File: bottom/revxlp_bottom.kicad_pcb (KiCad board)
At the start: 2 copper layers, 238.7 x 92.9 mm, 9 parts

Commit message: Initial 3dp case work.
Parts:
- moved H3 18.3 mm to (64.5, 99.7)
- moved H5 18.3 mm to (181.2, 125.8)
- moved H6 18.3 mm to (224.8, 99.7)
- moved H1 18.3 mm to (72.1, 66.2)
- moved H2 18.3 mm to (217.2, 66.2)
- moved rev41lp_edgecutPCB 18.3 mm to (144.6, 62.0)
- moved G*** 18.3 mm to (152.3, 67.1)
- moved H4 18.3 mm to (107.6, 126.2)
- moved H7 18.3 mm to (144.6, 78.1)
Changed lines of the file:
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@@
     )
     (pad_to_mask_clearance 0)
-    (aux_axis_origin 142.816164 156.58206)
     (grid_origin 110.242222 -34.443781)
     (pcbplotparams
-      (layerselection 0x00010fc_ffffffff)
+      (layerselection 0x0001000_7ffffffe)
       (disableapertmacros false)
       (usegerberextensions true)
@@
       (hpglpenspeed 20)
       (hpglpendiameter 15.000000)
-      (dxfpolygonmode true)
-      (dxfimperialunits true)
+      (dxfpolygonmode false)
+      (dxfimperialunits false)
       (dxfusepcbnewfont true)
       (psnegative false)
@@
       (sketchpadsonfab false)
       (subtractmaskfromsilk true)
-      (outputformat 1)
+      (outputformat 3)
       (mirror false)
       (drillshape 0)
       (scaleselection 1)
-      (outputdirectory "./")
+      (outputdirectory "./dxf")
     )
   )
@@
   (net 2 "+5V")
   (footprint "revxlp:rev41lp_edgecutBottomPlate" (layer "F.Cu")
-    (at 144.871005 43.697242)
+    (at 144.639118 61.979835)
     (attr through_hole)
     (fp_text reference "rev41lp_edgecutPCB" (at 0 0.5) (layer "F.SilkS") hide
@@
     (fp_arc (start -109.584369 0.795048) (mid -109.232514 0.237391) (end -108.61 0.019999) (layer "Edge.Cuts") (width 0.2))
     (fp_arc (start -55.237421 0.019999) (mid -52.973357 0.148562) (end -50.7384 0.532597) (layer "Edge.Cuts") (width 0.2))
-    (fp_arc (start 19.732403 86.445868) (mid 17.497445 86.829902) (end 15.233381 86.958468) (layer "Edge.Cuts") (width 0.2))
+    (fp_arc (start 19.732403 86.445868) (mid 17.497446 86.829906) (end 15.233381 86.958468) (layer "Edge.Cuts") (width 0.2))
     (fp_arc (start -100.034262 53.761991) (mid -102.298326 53.633428) (end -104.533283 53.249393) (layer "Edge.Cuts") (width 0.2))
     (fp_arc (start -17.78846 86.958467) (mid -20.052524 86.829904) (end -22.287481 86.445868) (layer "Edge.Cuts") (width 0.2))
@@
     (fp_arc (start 55.327513 75.76074) (mid 55.034606 76.467826) (end 54.327513 76.76074) (layer "Edge.Cuts") (width 0.2))
     (fp_arc (start -86.118211 53.76199) (mid -83.854147 53.890553) (end -81.619191 54.27459) (layer "Edge.Cuts") (width 0.2))
-    (fp_arc (start 48.183323 0.532598) (mid 50.418279 0.148565) (end 52.682343 0.02) (layer "Edge.Cuts") (width 0.2))
+    (fp_arc (start 48.183323 0.532598) (mid 50.418279 0.14856) (end 52.682343 0.02) (layer "Edge.Cuts") (width 0.2))
     (fp_arc (start 118.045976 48.513551) (mid 117.919653 49.268421) (end 117.296557 49.712872) (layer "Edge.Cuts") (width 0.2))
-    (fp_arc (start 101.978204 53.249393) (mid 99.743247 53.633427) (end 97.479183 53.761992) (layer "Edge.Cuts") (width 0.2))
+    (fp_arc (start 101.978204 53.249393) (mid 99.743248 53.633439) (end 97.479183 53.761992) (layer "Edge.Cuts") (width 0.2))
     (fp_arc (start 106.05492 0.019999) (mid 106.677424 0.237398) (end 107.029291 0.795047) (layer "Edge.Cuts") (width 0.2))
     (fp_arc (start 55.327512 60.550052) (mid 55.544915 59.927541) (end 56.102561 59.575682) (layer "Edge.Cuts") (width 0.2))
     (fp_arc (start -40.031514 82.349335) (mid -40.51367 82.082072) (end -40.780933 81.599916) (layer "Edge.Cuts") (width 0.2))
     (fp_arc (start -1.387482 -5.210371) (mid -0.943031 -5.833468) (end -0.188161 -5.959791) (layer "Edge.Cuts") (width 0.2))
-    (fp_arc (start 38.502691 2.749566) (mid 38.066137 2.799018) (end 37.628944 2.755581) (layer "Edge.Cuts") (width 0.2))
+    (fp_arc (start 38.502691 2.749566) (mid 38.066137 2.799039) (end 37.628944 2.755581) (layer "Edge.Cuts") (width 0.2))
     (fp_arc (start -4.911415 10.073644) (mid -5.353397 10.705476) (end -6.113507 10.835067) (layer "Edge.Cuts") (width 0.2))
-    (fp_arc (start 39.164133 77.535789) (mid 39.515979 76.978113) (end 40.138502 76.76074) (layer "Edge.Cuts") (width 0.2))
+    (fp_arc (start 39.164133 77.535789) (mid 39.516018 76.978179) (end 40.138502 76.76074) (layer "Edge.Cuts") (width 0.2))
     (fp_arc (start -42.693581 76.760738) (mid -42.071066 76.97813) (end -41.71921 77.535788) (layer "Edge.Cuts") (width 0.2))
   )
   (footprint "MountingHole:MountingHole_3.2mm_M3" (layer "B.Cu")
-    (at 225.018875 81.383061 180)
+    (at 224.786988 99.665654 180)
     (descr "Mounting Hole 3.2mm, no annular, M3")
     (tags "mounting hole 3.2mm no annular m3")
@@
   )
   (footprint "MountingHole:MountingHole_3.2mm_M3" (layer "B.Cu")
-    (at 144.87101 59.788938 180)
+    (at 144.639123 78.071531 180)
     (descr "Mounting Hole 3.2mm, no annular, M3")
     (tags "mounting hole 3.2mm no annular m3")
@@
   )
   (footprint "MountingHole:MountingHole_3.2mm_M3" (layer "B.Cu")
-    (at 107.842305 107.868103 180)
+    (at 107.610418 126.150696 180)
     (descr "Mounting Hole 3.2mm, no annular, M3")
     (tags "mounting hole 3.2mm no annular m3")
@@
   )
   (footprint "MountingHole:MountingHole_3.2mm_M3" (layer "B.Cu")
-    (at 181.392308 107.468103 180)
+    (at 181.160421 125.750696 180)
     (descr "Mounting Hole 3.2mm, no annular, M3")
     (tags "mounting hole 3.2mm no annular m3")
@@
   )
   (footprint "MountingHole:MountingHole_3.2mm_M3" (layer "B.Cu")
-    (at 217.400305 47.893104 180)
+    (at 217.168418 66.175697 180)
     (descr "Mounting Hole 3.2mm, no annular, M3")
     (tags "mounting hole 3.2mm no annular m3")
@@
   )
   (footprint "revxlp:Z_Towel_Logo" (layer "B.Cu")
-    (at 152.579849 48.779431 -103)
+    (at 152.347962 67.062024 -103)
     (attr through_hole)
     (fp_text reference "G***" (at 0 0 77) (layer "B.SilkS") hide
@@
   )
   (footprint "MountingHole:MountingHole_3.2mm_M3" (layer "B.Cu")
-    (at 64.722623 81.383061 180)
+    (at 64.490736 99.665654 180)
     (descr "Mounting Hole 3.2mm, no annular, M3")
     (tags "mounting hole 3.2mm no annular m3")
@@
   )
   (footprint "MountingHole:MountingHole_3.2mm_M3" (layer "B.Cu")
-    (at 72.342303 47.893105 180)
+    (at 72.110416 66.175698 180)
     (descr "Mounting Hole 3.2mm, no annular, M3")
     (tags "mounting hole 3.2mm no annular m3")
@@
     (polygon
       (pts
-        (xy 255.21352 28.48898)
-        (xy 272.713517 29.488977)
-        (xy 274.213519 136.988983)
-        (xy 144.213519 141.238978)
-        (xy 12.213516 109.238982)
-        (xy 32.463518 25.738984)
+        (xy 254.981633 46.771573)
+        (xy 272.48163 47.77157)
+        (xy 273.981632 155.271576)
+        (xy 143.981632 159.521571)
+        (xy 11.981629 127.521575)
+        (xy 32.231631 44.021577)
       )
     )
@@
     (polygon
       (pts
-        (xy 254.120178 27.221259)
-        (xy 276.370171 136.471261)
-        (xy 11.120169 131.471257)
-        (xy 36.62018 23.721262)
+        (xy 253.888291 45.503852)
+        (xy 276.138284 154.753854)
+        (xy 10.888282 149.75385)
+        (xy 36.388293 42.003855)
       )
     )

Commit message: Fixes for bottom plate and 3dp case to actually match PCB, add bottom edge fillet/chamfer.
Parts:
- moved G*** 6.53 mm to (146.0, 65.5)
- moved H1 1.30 mm to (73.4, 66.2)
- moved H3 1.30 mm to (65.8, 99.7)
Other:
- board size 238.7 x 92.9 mm -> 238.7 x 94.8 mm

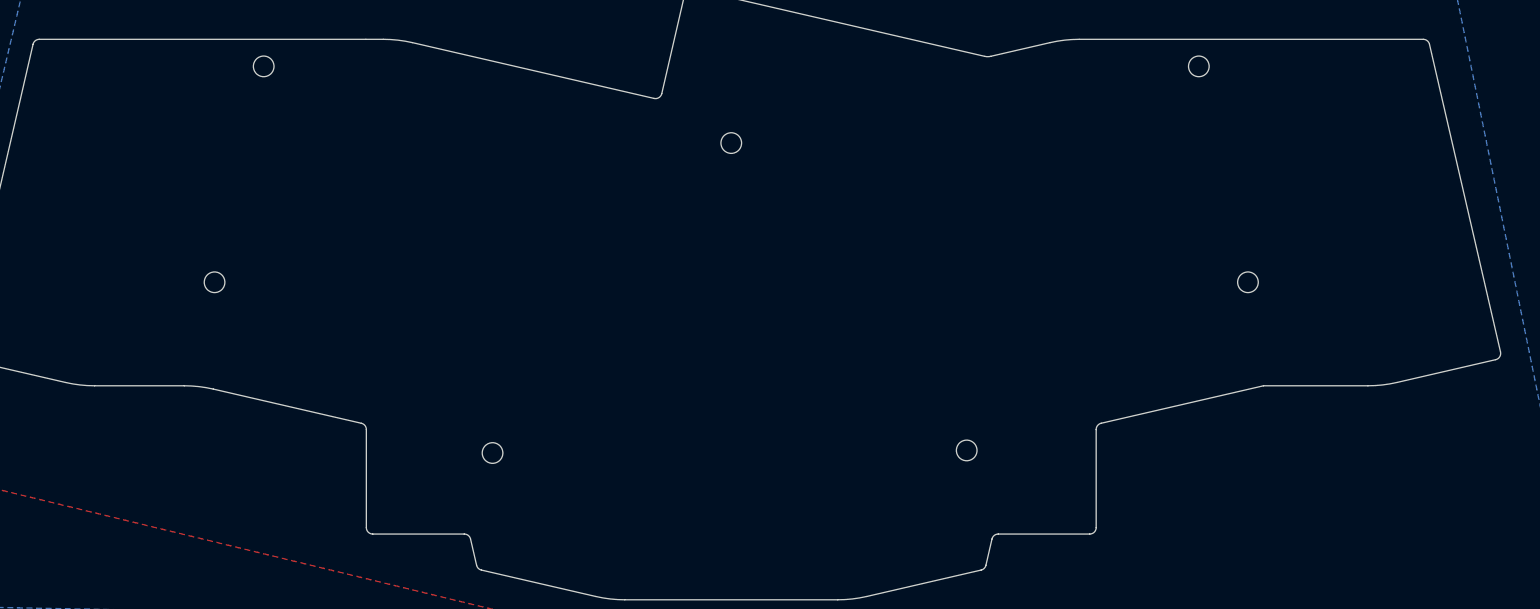
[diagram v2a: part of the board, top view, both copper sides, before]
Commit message: Enlarge and reposition bottom mounting holes.
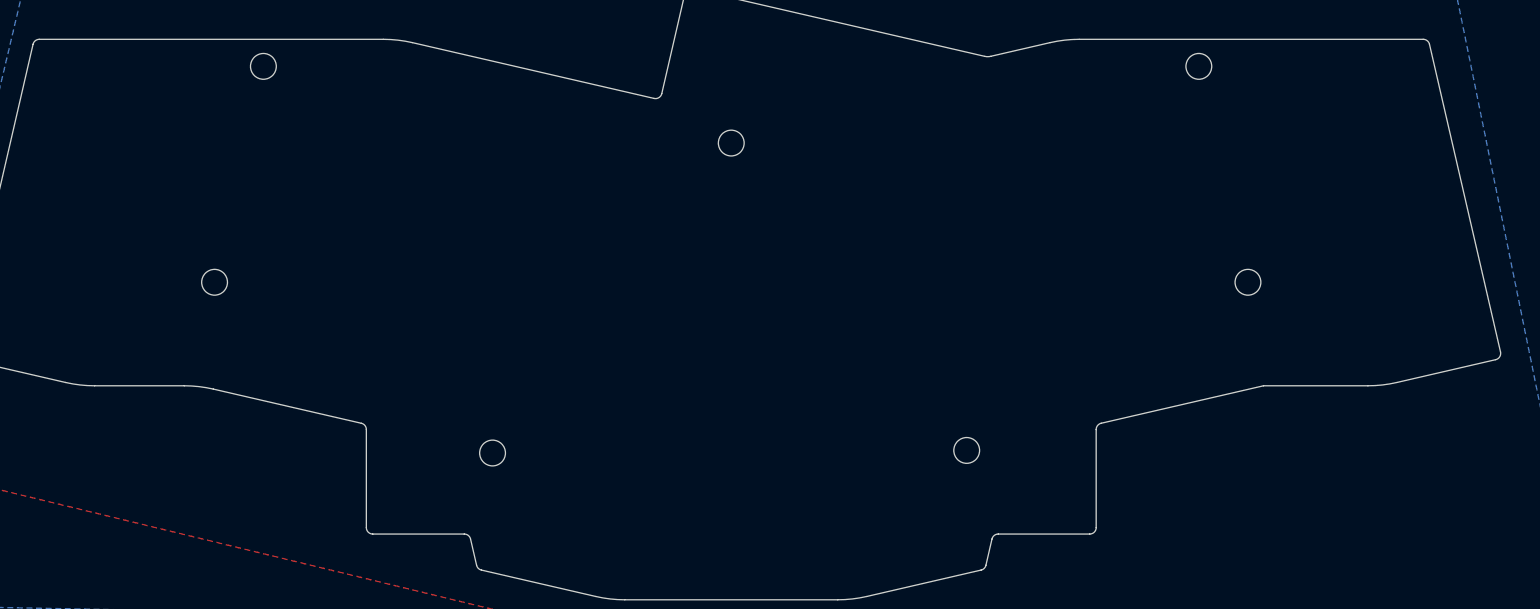
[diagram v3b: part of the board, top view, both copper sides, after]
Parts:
- H1, H2, H3, H4, H5, H6, H7: footprint MountingHole:MountingHole_3.2mm_M3 -> MountingHole:MountingHole_4mm
- moved H1 1.34 mm to (72.1, 66.2)
- moved H3 1.30 mm to (64.5, 99.7)
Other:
- outline, holes or cut-outs redrawn

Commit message: Fix position to match PCB so case gen works.
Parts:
- moved rev41lp_edgecutPCB 34.6 mm to (154.2, 28.8)
- moved H3 34.6 mm to (74.1, 66.5)
- moved H5 34.6 mm to (190.8, 92.5)
- moved H6 34.6 mm to (234.4, 66.5)
- moved H7 34.6 mm to (154.2, 44.9)
- moved H1 34.6 mm to (81.7, 33.0)
- moved H2 34.6 mm to (226.8, 33.0)
- moved H4 34.6 mm to (117.2, 92.9)
- moved G*** 9.59 mm to (155.6, 65.5)
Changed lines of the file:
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@@
   (net 2 "+5V")
   (footprint "revxlp:rev41lp_edgecutBottomPlate" (layer "F.Cu")
-    (at 144.639118 61.979835)
+    (at 154.229532 28.768286)
     (attr through_hole)
     (fp_text reference "rev41lp_edgecutPCB" (at 0 0.5) (layer "F.SilkS") hide
@@
     (fp_line (start -40.441671 77.515789) (end -39.503394 81.579917) (layer "Edge.Cuts") (width 0.2))
     (fp_arc (start 40.441672 77.515789) (mid 40.793521 76.958127) (end 41.416042 76.74074) (layer "Edge.Cuts") (width 0.2))
-    (fp_arc (start 49.460861 0.512599) (mid 51.695818 0.128562) (end 53.959882 0) (layer "Edge.Cuts") (width 0.2))
+    (fp_arc (start 49.460861 0.512599) (mid 51.695817 0.128557) (end 53.959882 0) (layer "Edge.Cuts") (width 0.2))
     (fp_arc (start -7.200363 -7.073925) (mid -6.757044 -7.696834) (end -6.003106 -7.823822) (layer "Edge.Cuts") (width 0.2))
     (fp_arc (start -84.840673 53.741991) (mid -82.576609 53.870554) (end -80.341652 54.25459) (layer "Edge.Cuts") (width 0.2))
     (fp_arc (start -16.510921 86.938468) (mid -18.774985 86.809905) (end -21.009942 86.425869) (layer "Edge.Cuts") (width 0.2))
-    (fp_arc (start 39.503394 81.579917) (mid 39.236738 82.062689) (end 38.753975 82.329336) (layer "Edge.Cuts") (width 0.2))
+    (fp_arc (start 39.503394 81.579917) (mid 39.236753 82.062704) (end 38.753975 82.329336) (layer "Edge.Cuts") (width 0.2))
     (fp_arc (start -10.776776 8.41722) (mid -11.221228 9.040317) (end -11.976099 9.166638) (layer "Edge.Cuts") (width 0.2))
     (fp_arc (start 56.605052 60.530052) (mid 56.822458 59.907551) (end 57.380101 59.555682) (layer "Edge.Cuts") (width 0.2))
@@
     (fp_arc (start 56.605052 75.74074) (mid 56.31206 76.447752) (end 55.605051 76.74074) (layer "Edge.Cuts") (width 0.2))
     (fp_arc (start -118.574096 49.692873) (mid -119.197193 49.248422) (end -119.323515 48.493552) (layer "Edge.Cuts") (width 0.2))
-    (fp_arc (start 103.255743 53.229393) (mid 101.020786 53.613425) (end 98.756722 53.741991) (layer "Edge.Cuts") (width 0.2))
+    (fp_arc (start 103.255743 53.229393) (mid 101.020786 53.613422) (end 98.756722 53.741991) (layer "Edge.Cuts") (width 0.2))
     (fp_arc (start -57.380101 59.555682) (mid -56.822443 59.907537) (end -56.605052 60.530052) (layer "Edge.Cuts") (width 0.2))
     (fp_arc (start -108.30683 0.775049) (mid -107.954975 0.217391) (end -107.33246 0) (layer "Edge.Cuts") (width 0.2))
-    (fp_arc (start 40.244726 2.638295) (mid 39.794418 2.693234) (end 39.343321 2.645225) (layer "Edge.Cuts") (width 0.2))
+    (fp_arc (start 40.244726 2.638295) (mid 39.79442 2.693222) (end 39.343321 2.645225) (layer "Edge.Cuts") (width 0.2))
     (fp_arc (start -98.756723 53.741992) (mid -101.020787 53.613429) (end -103.255744 53.229393) (layer "Edge.Cuts") (width 0.2))
     (fp_arc (start -38.753975 82.329336) (mid -39.236131 82.062073) (end -39.503394 81.579917) (layer "Edge.Cuts") (width 0.2))
     (fp_arc (start -41.416042 76.740739) (mid -40.793527 76.958131) (end -40.441671 77.515789) (layer "Edge.Cuts") (width 0.2))
-    (fp_arc (start 107.332459 0) (mid 107.954971 0.217385) (end 108.30683 0.775048) (layer "Edge.Cuts") (width 0.2))
+    (fp_arc (start 107.332459 0) (mid 107.954995 0.217376) (end 108.30683 0.775048) (layer "Edge.Cuts") (width 0.2))
     (fp_arc (start -55.605052 76.74074) (mid -56.312159 76.447847) (end -56.605052 75.74074) (layer "Edge.Cuts") (width 0.2))
     (fp_arc (start 21.009942 86.425869) (mid 18.774985 86.809904) (end 16.510921 86.938468) (layer "Edge.Cuts") (width 0.2))
-    (fp_arc (start 119.323515 48.493552) (mid 119.19719 49.24841) (end 118.574096 49.692873) (layer "Edge.Cuts") (width 0.2))
+    (fp_arc (start 119.323515 48.493552) (mid 119.197193 49.248429) (end 118.574096 49.692873) (layer "Edge.Cuts") (width 0.2))
   )
   (footprint "MountingHole:MountingHole_4mm" (layer "B.Cu")
-    (at 224.786988 99.665654 180)
+    (at 234.377402 66.454105 180)
     (descr "Mounting Hole 4mm, no annular")
     (tags "mounting hole 4mm no annular")
@@
   )
   (footprint "MountingHole:MountingHole_4mm" (layer "B.Cu")
-    (at 144.639123 78.071532 180)
+    (at 154.229537 44.859983 180)
     (descr "Mounting Hole 4mm, no annular")
     (tags "mounting hole 4mm no annular")
@@
   )
   (footprint "MountingHole:MountingHole_4mm" (layer "B.Cu")
-    (at 107.610418 126.150696 180)
+    (at 117.200832 92.939147 180)
     (descr "Mounting Hole 4mm, no annular")
     (tags "mounting hole 4mm no annular")
@@
   )
   (footprint "MountingHole:MountingHole_4mm" (layer "B.Cu")
-    (at 181.160421 125.750697 180)
+    (at 190.750835 92.539148 180)
     (descr "Mounting Hole 4mm, no annular")
     (tags "mounting hole 4mm no annular")
@@
   )
   (footprint "MountingHole:MountingHole_4mm" (layer "B.Cu")
-    (at 217.168415 66.175697 180)
+    (at 226.758829 32.964148 180)
     (descr "Mounting Hole 4mm, no annular")
     (tags "mounting hole 4mm no annular")
@@
   )
   (footprint "revxlp:Z_Towel_Logo" (layer "B.Cu")
-    (at 145.998067 65.530604 -103)
+    (at 155.588481 65.530604 -103)
     (attr through_hole)
     (fp_text reference "G***" (at 0 0 77) (layer "B.SilkS") hide
@@
   )
   (footprint "MountingHole:MountingHole_4mm" (layer "B.Cu")
-    (at 64.490736 99.665654 180)
+    (at 74.08115 66.454105 180)
     (descr "Mounting Hole 4mm, no annular")
     (tags "mounting hole 4mm no annular")
@@
   )
   (footprint "MountingHole:MountingHole_4mm" (layer "B.Cu")
-    (at 72.065416 66.175698 180)
+    (at 81.65583 32.964149 180)
     (descr "Mounting Hole 4mm, no annular")
     (tags "mounting hole 4mm no annular")
@@
     (polygon
       (pts
-        (xy 256.278633 46.771573)
-        (xy 273.77863 47.77157)
-        (xy 275.278632 155.271576)
-        (xy 145.278632 159.521571)
-        (xy 13.278629 127.521575)
-        (xy 33.528631 44.021577)
+        (xy 256.278633 13.560024)
+        (xy 273.77863 14.560021)
+        (xy 275.278632 122.060027)
+        (xy 145.278632 126.310022)
+        (xy 13.278629 94.310026)
+        (xy 33.528631 10.810028)
       )
     )
@@
     (polygon
       (pts
-        (xy 255.185291 45.503852)
-        (xy 277.435284 154.753854)
-        (xy 12.185282 149.75385)
-        (xy 37.685293 42.003855)
+        (xy 277.892222 12.931219)
+        (xy 277.435284 121.542305)
+        (xy 12.185282 116.542301)
+        (xy 37.685293 8.792306)
       )
     )

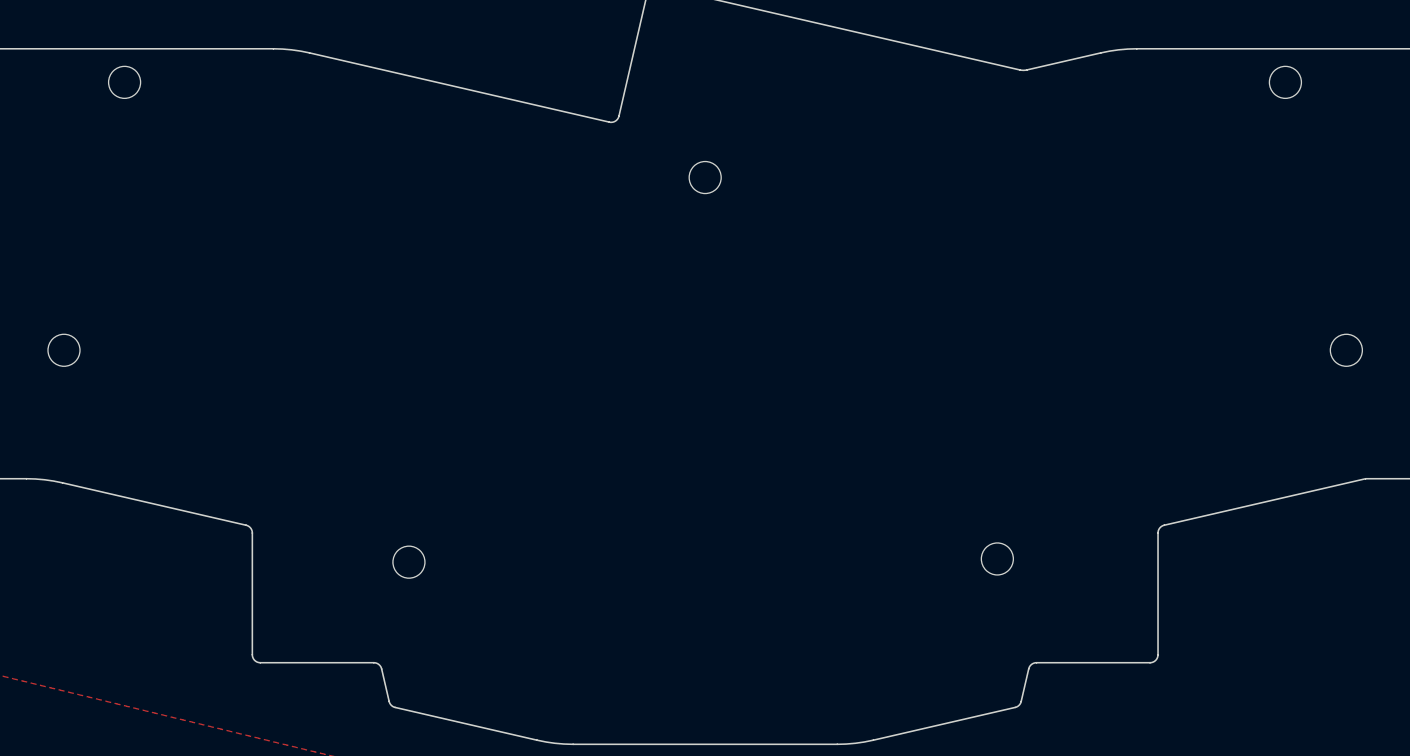
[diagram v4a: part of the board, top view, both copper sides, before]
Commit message: Move to M2 mounting hardware.
* New M2 footprint.
* Switch to M2 LCSC part number.
* Smaller holes in the case.
* Adjust the bottom plate hole size.
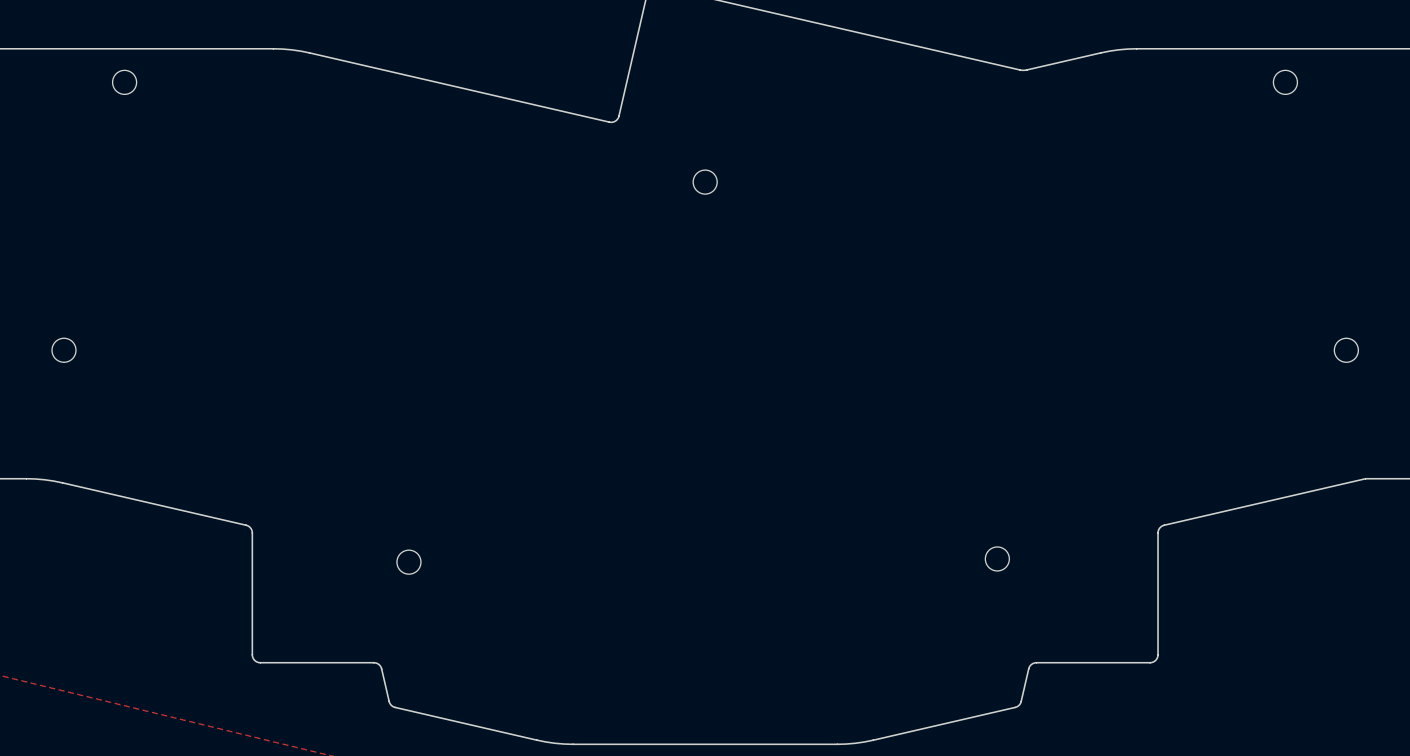
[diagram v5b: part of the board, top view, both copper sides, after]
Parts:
- H1, H2, H3, H4, H5, H6, H7: footprint MountingHole:MountingHole_4mm -> MountingHole:MountingHole_3mm
- moved H7 0.57 mm to (154.2, 45.4)
